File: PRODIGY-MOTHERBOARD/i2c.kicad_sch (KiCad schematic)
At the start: 7 parts, among them U7 PCA9306DC, U8 SN74LVC1T45DBV

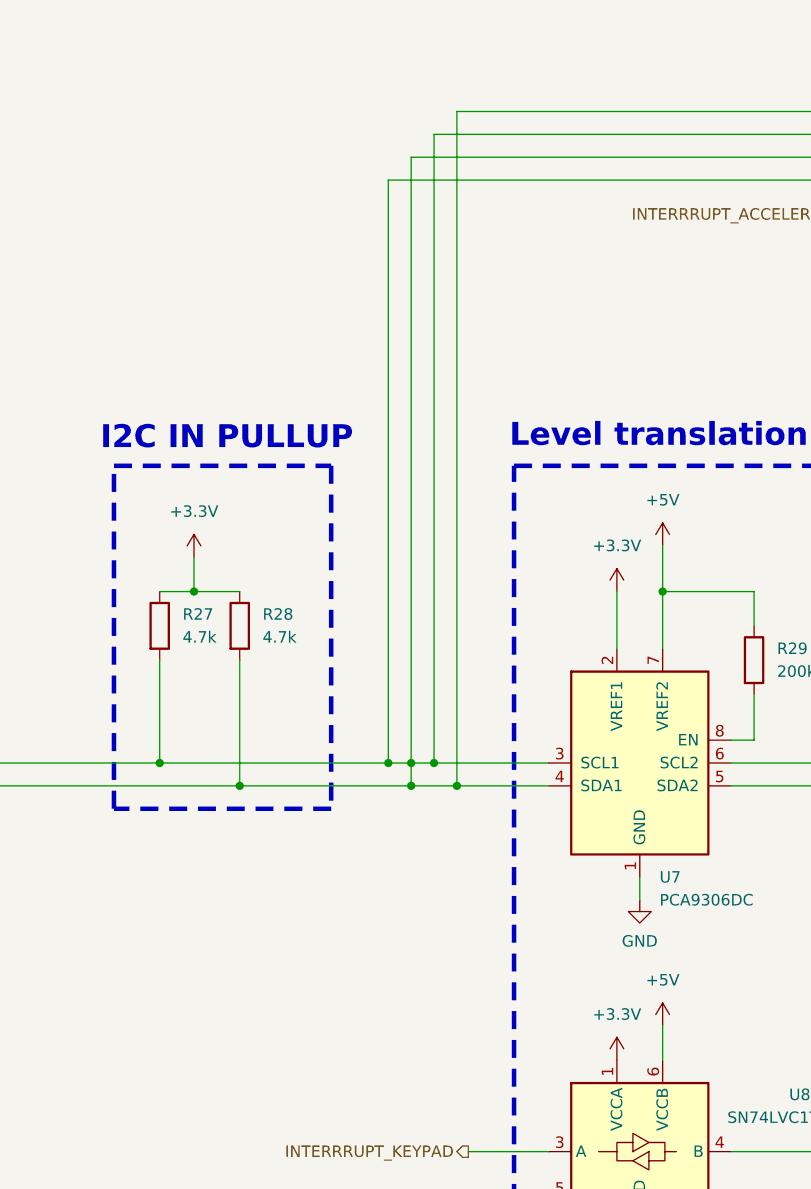
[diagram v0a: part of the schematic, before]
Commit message: Motherboard footprints assigned.
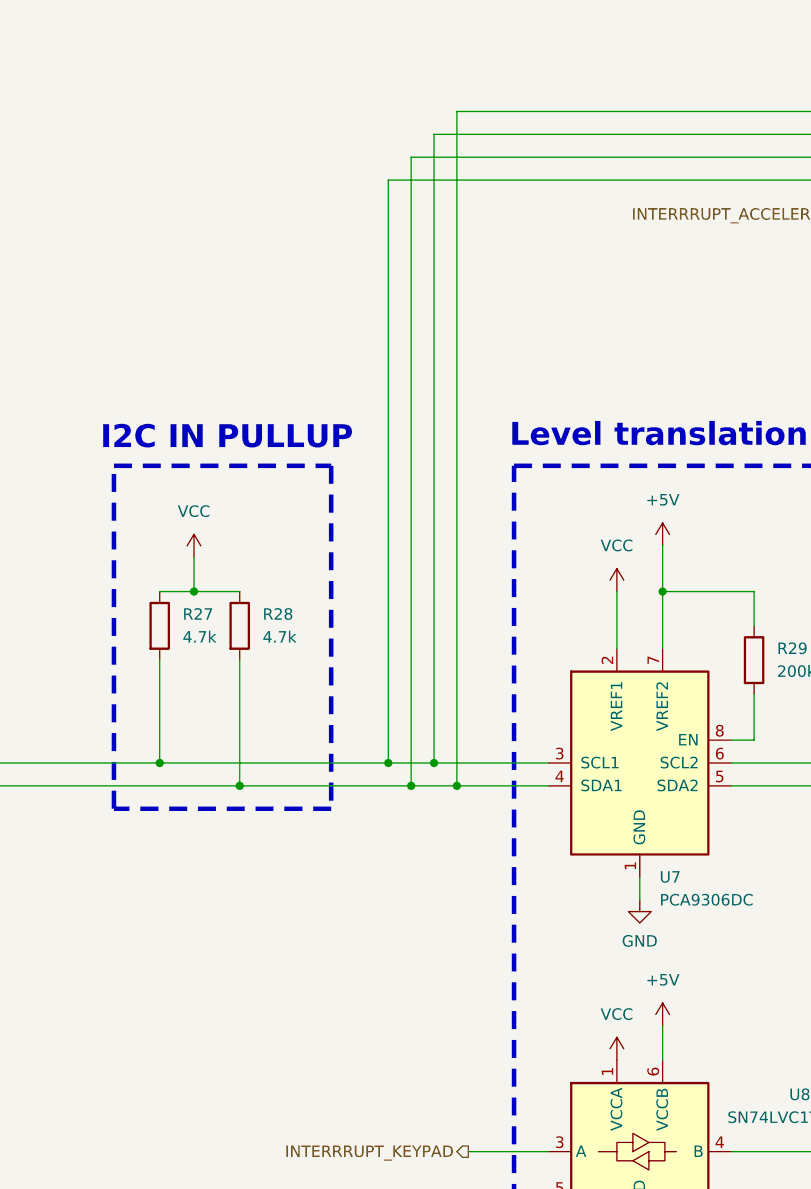
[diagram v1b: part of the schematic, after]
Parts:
- R27, R28, R29, R30, R31: footprint (none) -> Resistor_SMD:R_0603_1608Metric
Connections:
- net I2C_SCL: no longer R28.2, U7.4 (SDA1)
- net +3.3V renamed VCC
- new net I2C_SDA: R28.2, U7.4 (SDA1)

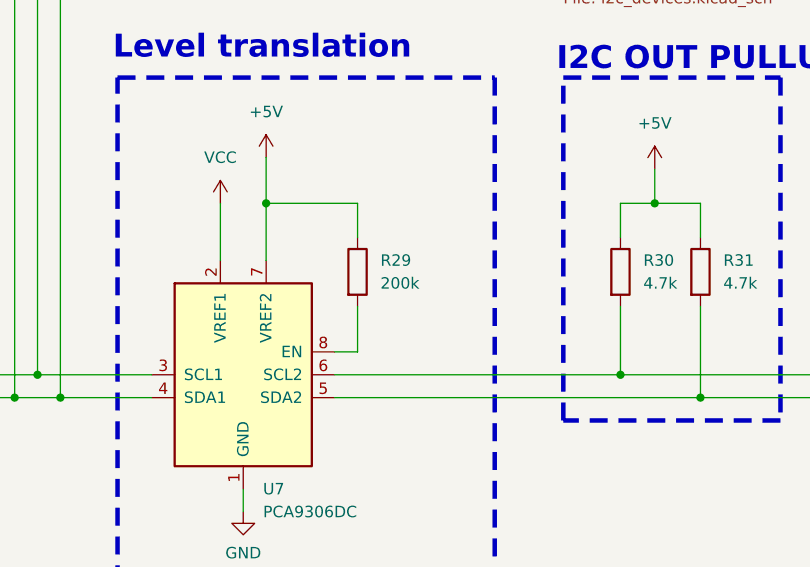
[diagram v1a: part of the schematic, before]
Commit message: finished motherboard bom and updated footprints
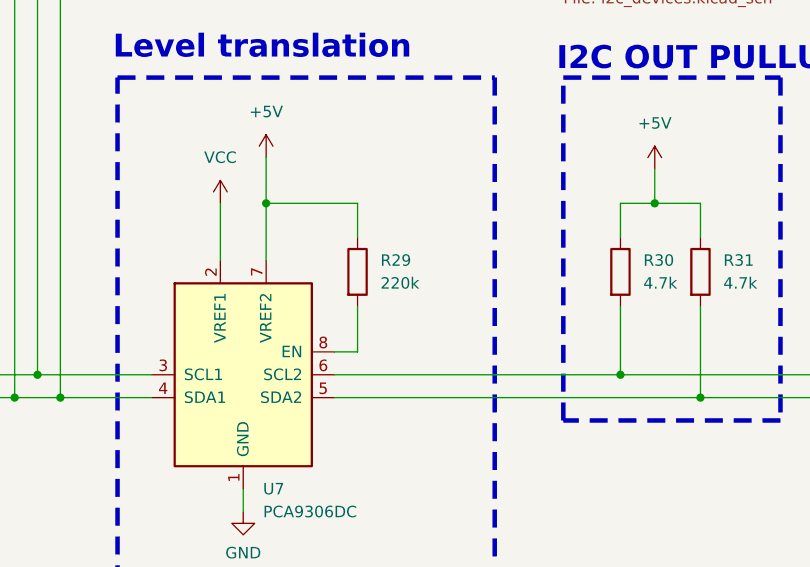
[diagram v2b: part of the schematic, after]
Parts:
- R27, R28, R30, R31: TME (none) -> CRCW06034K70FKTABC
- R29: value 200k -> 220k; TME (none) -> ERJ3EKF2203V
- U7: TME (none) -> PCA9306DCTR
- U8: TME (none) -> SN74LVC1T45DBVR
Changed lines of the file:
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@@
 			)
 		)
-		(property "TME" ""
+		(property "TME" "SN74LVC1T45DBVR"
 			(at 130.81 149.86 0)
 			(effects
@@
 			)
 		)
-		(property "TME" ""
+		(property "TME" "PCA9306DCTR"
 			(at 130.81 106.68 0)
 			(effects
@@
 			)
 		)
-		(property "TME" ""
+		(property "TME" "CRCW06034K70FKTABC "
 			(at 181.61 95.25 0)
 			(effects
@@
 			)
 		)
-		(property "TME" ""
+		(property "TME" "CRCW06034K70FKTABC "
 			(at 86.36 91.44 0)
 			(effects
@@
 			)
 		)
-		(property "TME" ""
+		(property "TME" "CRCW06034K70FKTABC "
 			(at 172.72 95.25 0)
 			(effects
@@
 			)
 		)
-		(property "Value" "200k"
+		(property "Value" "220k"
 			(at 146.05 96.5199 0)
 			(effects
@@
 			)
 		)
-		(property "TME" ""
+		(property "TME" "ERJ3EKF2203V"
 			(at 143.51 95.25 0)
 			(effects
@@
 			)
 		)
-		(property "TME" ""
+		(property "TME" "CRCW06034K70FKTABC "
 			(at 77.47 91.44 0)
 			(effects

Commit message: Analog lazout done
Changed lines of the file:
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@@
+	(wire
+		(pts
+			(xy 54.61 106.68) (xy 77.47 106.68)
+		)
+		(stroke
+			(width 0)
+			(type default)
+		)
+	)
 	(wire
 		(pts
@@
 	(wire
 		(pts
-			(xy 59.69 106.68) (xy 77.47 106.68)
-		)
-		(stroke
-			(width 0)
-			(type default)
-		)
-	)
-	(wire
-		(pts
 			(xy 172.72 87.63) (xy 176.53 87.63)
 		)
@@
 	(wire
 		(pts
-			(xy 59.69 109.22) (xy 86.36 109.22)
+			(xy 54.61 109.22) (xy 86.36 109.22)
 		)
 		(stroke
@@
 		)
 	)
+	(label "I2C_SCL_3V3"
+		(at 57.15 106.68 0)
+		(fields_autoplaced yes)
+		(effects
+			(font
+				(size 1.27 1.27)
+			)
+			(justify left bottom)
+		)
+	)
+	(label "I2C_SDA_5V"
+		(at 223.52 109.22 0)
+		(fields_autoplaced yes)
+		(effects
+			(font
+				(size 1.27 1.27)
+			)
+			(justify left bottom)
+		)
+	)
+	(label "I2C_SCL_5V"
+		(at 223.52 106.68 0)
+		(fields_autoplaced yes)
+		(effects
+			(font
+				(size 1.27 1.27)
+			)
+			(justify left bottom)
+		)
+	)
+	(label "I2C_SDA_3V3"
+		(at 57.15 109.22 0)
+		(fields_autoplaced yes)
+		(effects
+			(font
+				(size 1.27 1.27)
+			)
+			(justify left bottom)
+		)
+	)
 	(hierarchical_label "I2C_SCL"
 		(shape bidirectional)
-		(at 59.69 106.68 180)
+		(at 54.61 106.68 180)
 		(fields_autoplaced yes)
 		(effects
@@
 	(hierarchical_label "I2C_SDA"
 		(shape bidirectional)
-		(at 59.69 109.22 180)
+		(at 54.61 109.22 180)
 		(fields_autoplaced yes)
 		(effects
